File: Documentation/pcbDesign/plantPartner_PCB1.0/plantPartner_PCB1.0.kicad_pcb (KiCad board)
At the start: 2 copper layers, 148.3 x 66.8 mm, 78 parts, among them IC1 MPM3610, J1 Conn_01x04, J10 Screw_Terminal_01x03, J11 Conn_01x02, J12 Conn_01x03, J13 Conn_01x03, J14 Conn_01x03, J15 Conn_01x03, J16 Conn_01x04, J17 Conn_01x03, J18 Screw_Terminal_01x02, J19 Barrel_Jack, J2 Conn_01x04, J20 Conn_02x04_Top_Bottom, J21 Conn_01x04, J22 Conn_01x04, J23 Conn_01x01, J24 Conn_01x03, J25 Conn_01x03, J26 Conn_01x01, J27 Conn_01x01, J28 Conn_01x01, J29 Conn_01x02, J3 Conn_01x04, J4 Screw_Terminal, J5 Conn_01x02, J6 Screw_Terminal_01x03, J7 Conn_01x03, J8 Conn_02x04_Top_Bottom, J9 Conn_01x03, K1 SRD-05VDC-SL-C, K2 SRD-05VDC-SL-C, Q1 PNP, Q2 PNP, U1 EL357N-G, U2 MAX485, U3 ESP32-DEVKIT-V1, U4 EL357N-G

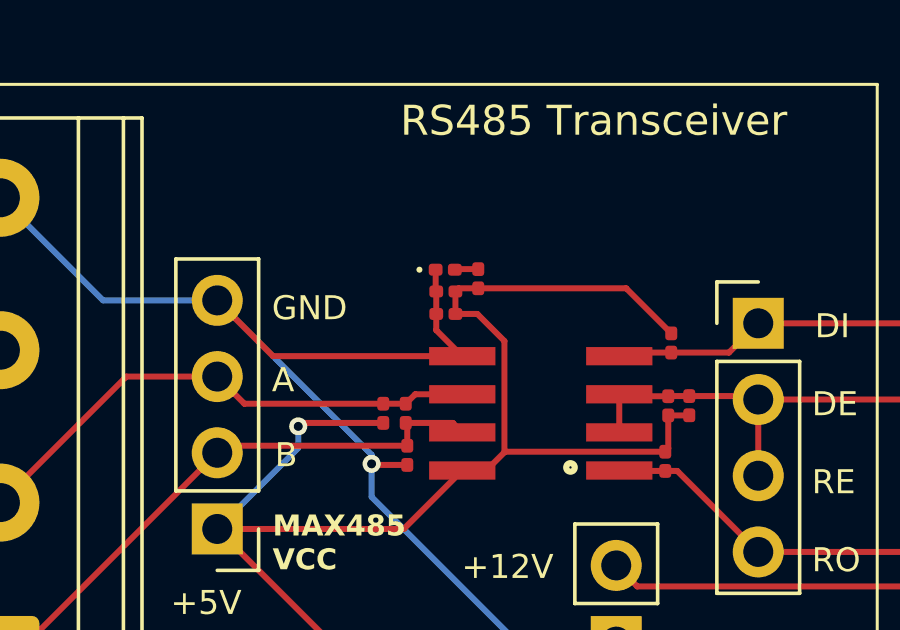
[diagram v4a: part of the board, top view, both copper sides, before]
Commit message: Meeting with Tyler. I tried to implement Lamp Circuit with MOSFET but having trouble simulating it in LTspice
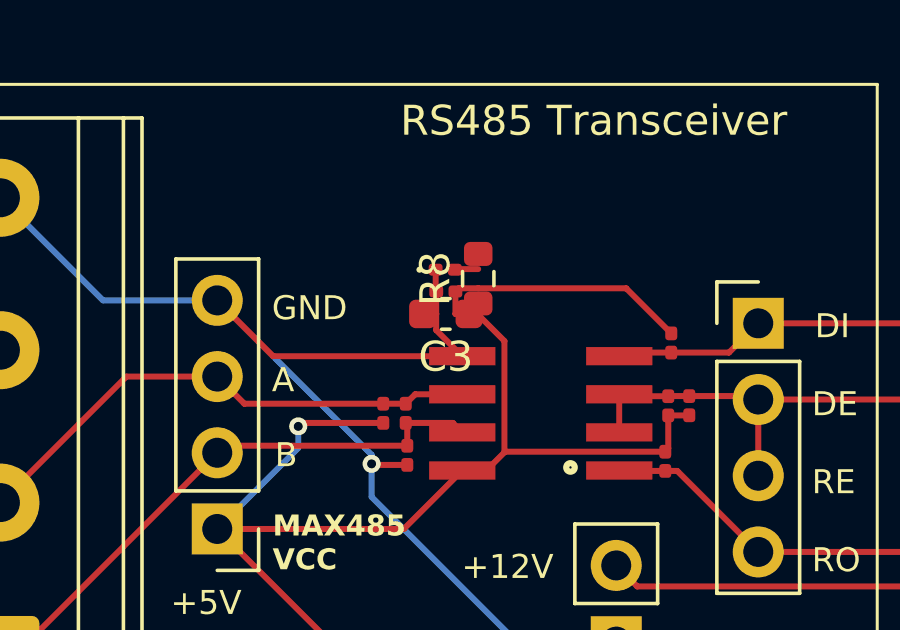
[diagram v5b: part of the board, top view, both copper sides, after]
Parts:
- C3: footprint Capacitor_SMD:C_0201_0603Metric -> Capacitor_SMD:C_0603_1608Metric
- R8: footprint Resistor_SMD:R_0201_0603Metric -> Resistor_SMD:R_0603_1608Metric
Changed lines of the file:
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@@
 		)
 	)
-	(footprint "Resistor_SMD:R_0201_0603Metric"
+	(footprint "Resistor_SMD:R_0603_1608Metric"
 		(layer "F.Cu")
 		(at 90.055 68.6275 90)
-		(descr "Resistor SMD 0201 (0603 Metric), square (rectangular) end terminal, IPC-7351 nominal, (Body size source: https://www.vishay.com/docs/20052/crcw0201e3.pdf), generated with kicad-footprint-generator")
+		(descr "Resistor SMD 0603 (1608 Metric), square (rectangular) end terminal, IPC-7351 nominal, (Body size source: IPC-SM-782 page 72, https://www.pcb-3d.com/wordpress/wp-content/uploads/ipc-sm-782a_amendment_1_and_2.pdf), generated with kicad-footprint-generator")
 		(tags "resistor")
 		(property "Reference" "R8"
-			(at 0 -1.05 90)
-			(layer "F.SilkS")
-			(hide yes)
+			(at 0 -1.43 90)
+			(layer "F.SilkS")
 			(effects
 				(font
@@
 		)
 		(property "Value" "1k"
-			(at 0 1.05 90)
+			(at 0 1.43 90)
 			(layer "F.Fab")
 			(effects
@@
 		(sheetfile "plantPartner_PCB1.0.kicad_sch")
 		(attr smd)
-		(fp_rect
-			(start -0.7 -0.35)
-			(end 0.7 0.35)
+		(fp_line
+			(start -0.237258 -0.5225)
+			(end 0.237258 -0.5225)
+			(stroke
+				(width 0.12)
+				(type solid)
+			)
+			(layer "F.SilkS")
+		)
+		(fp_line
+			(start -0.237258 0.5225)
+			(end 0.237258 0.5225)
+			(stroke
+				(width 0.12)
+				(type solid)
+			)
+			(layer "F.SilkS")
+		)
+		(fp_rect
+			(start -1.48 -0.73)
+			(end 1.48 0.73)
 			(stroke
 				(width 0.05)
@@
 		)
 		(fp_rect
-			(start -0.3 -0.15)
-			(end 0.3 0.15)
+			(start -0.8 -0.4125)
+			(end 0.8 0.4125)
 			(stroke
 				(width 0.1)
@@
 		)
 		(fp_text user "${REFERENCE}"
-			(at 0 -0.68 90)
-			(layer "F.Fab")
-			(effects
-				(font
-					(size 0.25 0.25)
-					(thickness 0.04)
-				)
-			)
-		)
-		(pad "" smd roundrect
-			(at -0.345 0 90)
-			(size 0.318 0.36)
-			(layers "F.Paste")
-			(roundrect_rratio 0.25)
-		)
-		(pad "" smd roundrect
-			(at 0.345 0 90)
-			(size 0.318 0.36)
-			(layers "F.Paste")
-			(roundrect_rratio 0.25)
+			(at 0 0 90)
+			(layer "F.Fab")
+			(effects
+				(font
+					(size 0.4 0.4)
+					(thickness 0.06)
+				)
+			)
 		)
 		(pad "1" smd roundrect
-			(at -0.32 0 90)
-			(size 0.46 0.4)
-			(layers "F.Cu" "F.Mask")
+			(at -0.825 0 90)
+			(size 0.8 0.95)
+			(layers "F.Cu" "F.Mask" "F.Paste")
 			(roundrect_rratio 0.25)
 			(net 52 "+5V")
@@
 		)
 		(pad "2" smd roundrect
-			(at 0.32 0 90)
-			(size 0.46 0.4)
-			(layers "F.Cu" "F.Mask")
+			(at 0.825 0 90)
+			(size 0.8 0.95)
+			(layers "F.Cu" "F.Mask" "F.Paste")
 			(roundrect_rratio 0.25)
 			(net 2 "Net-(D1-A)")
@@
 		)
 		(embedded_fonts no)
-		(model "${KICAD9_3DMODEL_DIR}/Resistor_SMD.3dshapes/R_0201_0603Metric.step"
+		(model "${KICAD9_3DMODEL_DIR}/Resistor_SMD.3dshapes/R_0603_1608Metric.step"
 			(offset
 				(xyz 0 0 0)
@@
 		)
 	)
-	(footprint "Capacitor_SMD:C_0201_0603Metric"
+	(footprint "Capacitor_SMD:C_0603_1608Metric"
 		(layer "F.Cu")
 		(at 88.975 69.8025 180)
-		(descr "Capacitor SMD 0201 (0603 Metric), square (rectangular) end terminal, IPC-7351 nominal, (Body size source: https://www.vishay.com/docs/20052/crcw0201e3.pdf), generated with kicad-footprint-generator")
+		(descr "Capacitor SMD 0603 (1608 Metric), square (rectangular) end terminal, IPC-7351 nominal, (Body size source: IPC-SM-782 page 76, https://www.pcb-3d.com/wordpress/wp-content/uploads/ipc-sm-782a_amendment_1_and_2.pdf), generated with kicad-footprint-generator")
 		(tags "capacitor")
 		(property "Reference" "C3"
-			(at 0 -1.05 0)
-			(layer "F.SilkS")
-			(hide yes)
+			(at 0 -1.43 180)
+			(layer "F.SilkS")
 			(effects
 				(font
@@
 		)
 		(property "Value" "10uF"
-			(at 0.285 1.05 0)
+			(at 0 1.43 180)
 			(layer "F.Fab")
 			(effects
@@
 		)
 		(property "Datasheet" "~"
-			(at 0 0 0)
+			(at 0 0 180)
 			(layer "F.Fab")
 			(hide yes)
@@
 		)
 		(property "Description" "Unpolarized capacitor"
-			(at 0 0 0)
+			(at 0 0 180)
 			(layer "F.Fab")
 			(hide yes)
@@
 		(sheetfile "plantPartner_PCB1.0.kicad_sch")
 		(attr smd)
-		(fp_rect
-			(start -0.7 -0.35)
-			(end 0.7 0.35)
+		(fp_line
+			(start -0.14058 0.51)
+			(end 0.14058 0.51)
+			(stroke
+				(width 0.12)
+				(type solid)
+			)
+			(layer "F.SilkS")
+		)
+		(fp_line
+			(start -0.14058 -0.51)
+			(end 0.14058 -0.51)
+			(stroke
+				(width 0.12)
+				(type solid)
+			)
+			(layer "F.SilkS")
+		)
+		(fp_rect
+			(start -1.48 -0.73)
+			(end 1.48 0.73)
 			(stroke
 				(width 0.05)
@@
 		)
 		(fp_rect
-			(start -0.3 -0.15)
-			(end 0.3 0.15)
+			(start -0.8 -0.4)
+			(end 0.8 0.4)
 			(stroke
 				(width 0.1)
@@
 		)
 		(fp_text user "${REFERENCE}"
-			(at 0 -0.68 0)
-			(layer "F.Fab")
-			(effects
-				(font
-					(size 0.25 0.25)
-					(thickness 0.04)
-				)
-			)
-		)
-		(pad "" smd roundrect
-			(at -0.345 0 180)
-			(size 0.318 0.36)
-			(layers "F.Paste")
-			(roundrect_rratio 0.25)
-		)
-		(pad "" smd roundrect
-			(at 0.345 0 180)
-			(size 0.318 0.36)
-			(layers "F.Paste")
-			(roundrect_rratio 0.25)
+			(at 0 0 180)
+			(layer "F.Fab")
+			(effects
+				(font
+					(size 0.4 0.4)
+					(thickness 0.06)
+				)
+			)
 		)
 		(pad "1" smd roundrect
-			(at -0.32 0 180)
-			(size 0.46 0.4)
-			(layers "F.Cu" "F.Mask")
+			(at -0.775 0 180)
+			(size 0.9 0.95)
+			(layers "F.Cu" "F.Mask" "F.Paste")
 			(roundrect_rratio 0.25)
 			(net 52 "+5V")
@@
 		)
 		(pad "2" smd roundrect
-			(at 0.32 0 180)
-			(size 0.46 0.4)
-			(layers "F.Cu" "F.Mask")
+			(at 0.775 0 180)
+			(size 0.9 0.95)
+			(layers "F.Cu" "F.Mask" "F.Paste")
 			(roundrect_rratio 0.25)
 			(net 1 "GND")
@@
 		)
 		(embedded_fonts no)
-		(model "${KICAD9_3DMODEL_DIR}/Capacitor_SMD.3dshapes/C_0201_0603Metric.step"
+		(model "${KICAD9_3DMODEL_DIR}/Capacitor_SMD.3dshapes/C_0603_1608Metric.step"
 			(offset
 				(xyz 0 0 0)

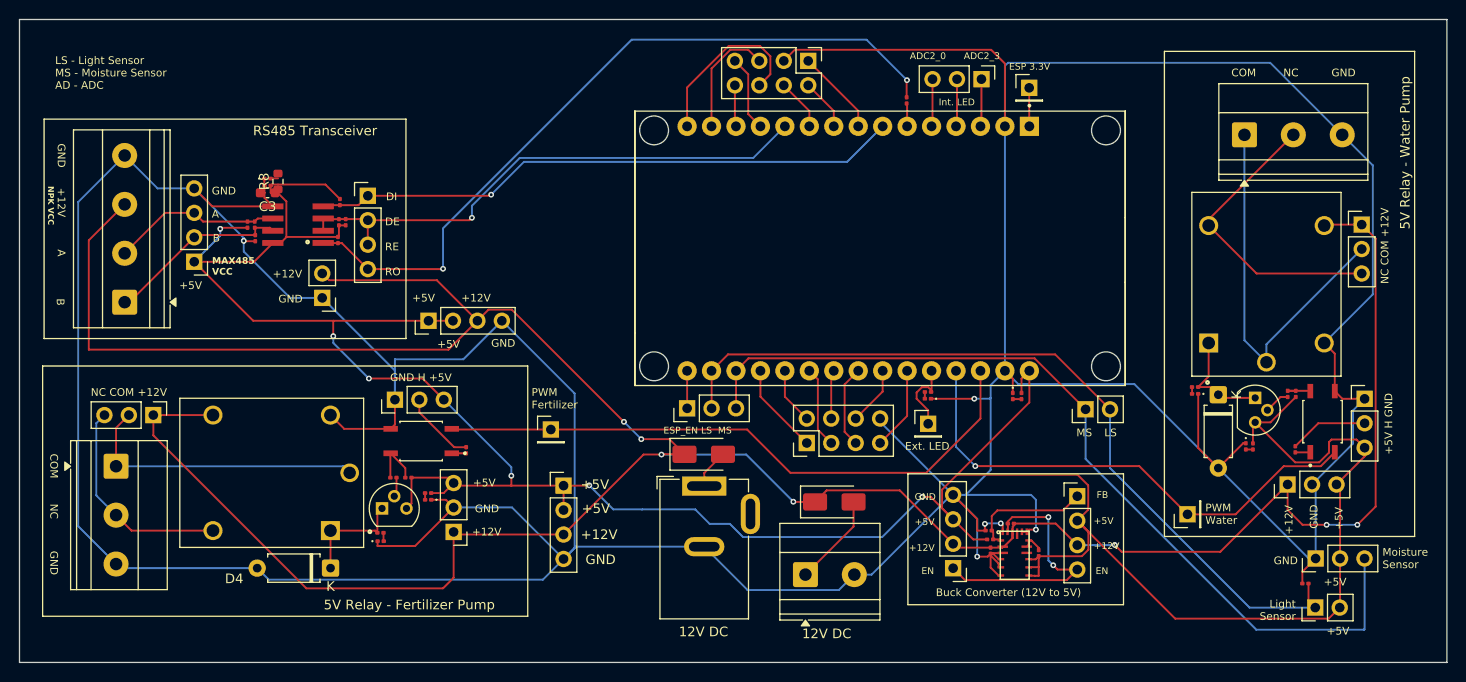
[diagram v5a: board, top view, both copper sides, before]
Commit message: Added Lamp to PCB. Added Copper Pours and Drill Holes. Now fixing rude error about cap. not getting copper pour connection properly
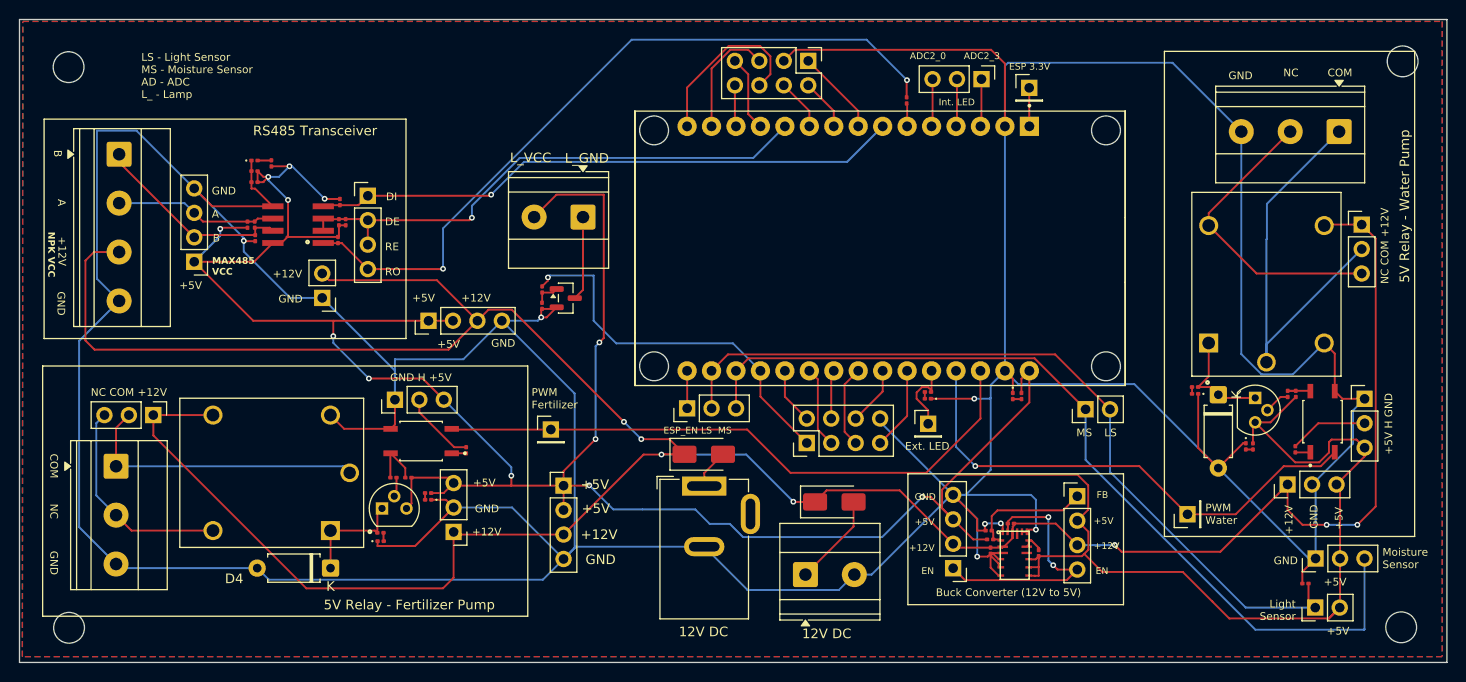
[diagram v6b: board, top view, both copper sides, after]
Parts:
- added J30: Screw_Terminal_01x02, TerminalBlock_Phoenix:TerminalBlock_Phoenix_MKDS-1,5-2-5.08_1x02_P5.08mm_Horizontal, F.Cu at (121.7, 72.3)
- added Q4: AO3400A, Package_TO_SOT_SMD:SOT-23, F.Cu at (120.0, 80.8)
- added R25: 100, Resistor_SMD:R_0201_0603Metric, F.Cu at (117.5, 79.8)
- added R27: 10k, Resistor_SMD:R_0201_0603Metric, F.Cu at (117.5, 81.5)
- added REF**: MountingHole_3.2mm_M3, MountingHole:MountingHole_3.2mm_M3, F.Cu at (68.3, 56.8)
- added REF**: MountingHole_3.2mm_M3, MountingHole:MountingHole_3.2mm_M3, F.Cu at (206.9, 56.1)
- added REF**: MountingHole_3.2mm_M3, MountingHole:MountingHole_3.2mm_M3, F.Cu at (68.3, 115.0)
- added REF**: MountingHole_3.2mm_M3, MountingHole:MountingHole_3.2mm_M3, F.Cu at (206.8, 115.0)
- C3: footprint Capacitor_SMD:C_0603_1608Metric -> Capacitor_SMD:C_0201_0603Metric
- R8: footprint Resistor_SMD:R_0603_1608Metric -> Resistor_SMD:R_0201_0603Metric
- moved J4 15.4 mm to (73.5, 65.8), turned to -90 degrees
- moved J10 9.84 mm to (200.3, 63.5), turned to 180 degrees
- moved D1 2.30 mm to (87.6, 66.5)
- moved C4 2.02 mm to (87.6, 67.5)
- moved R8 2.00 mm to (89.4, 66.8)
- moved C3 1.75 mm to (87.6, 68.7)
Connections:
- net /ADC1_6 renamed /LAMP_PIN
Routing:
- net +5V: track 298.6 -> 346.7 mm, vias 6 -> 12
- net /LAMP_PIN: track 9.49 -> 39.7 mm, vias 0 -> 1
- net GND: track 565.6 -> 583.1 mm, vias 6 -> 7
- net /Drain: track 0.00 -> 8.78 mm
- net +12V: track 307.4 -> 303.7 mm
- net /Gate: track 0.00 -> 2.73 mm
- net /COM: track 71.1 -> 73.6 mm
- net /B: track 19.2 -> 21.1 mm
- net /A: track 17.6 -> 16.9 mm
- net Net-(D1-A): track 0.79 -> 1.47 mm
- added copper zone on B.Cu, net GND
- added copper zone on F.Cu, net GND
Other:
- board text added: "AD2_7 AD2_8 AD1_4 L_PIN"
- board text added: "LS - Light Sensor MS - Moisture Sensor AD - ADC L_ - Lamp"
- board text added: "L_GND"
- board text added: "L_VCC"
- board text added: "R25"
- board text removed: "AD2_7 AD2_8 AD1_4 AD1_6"
- board text removed: "LS - Light Sensor MS - Moisture Sensor AD - ADC"

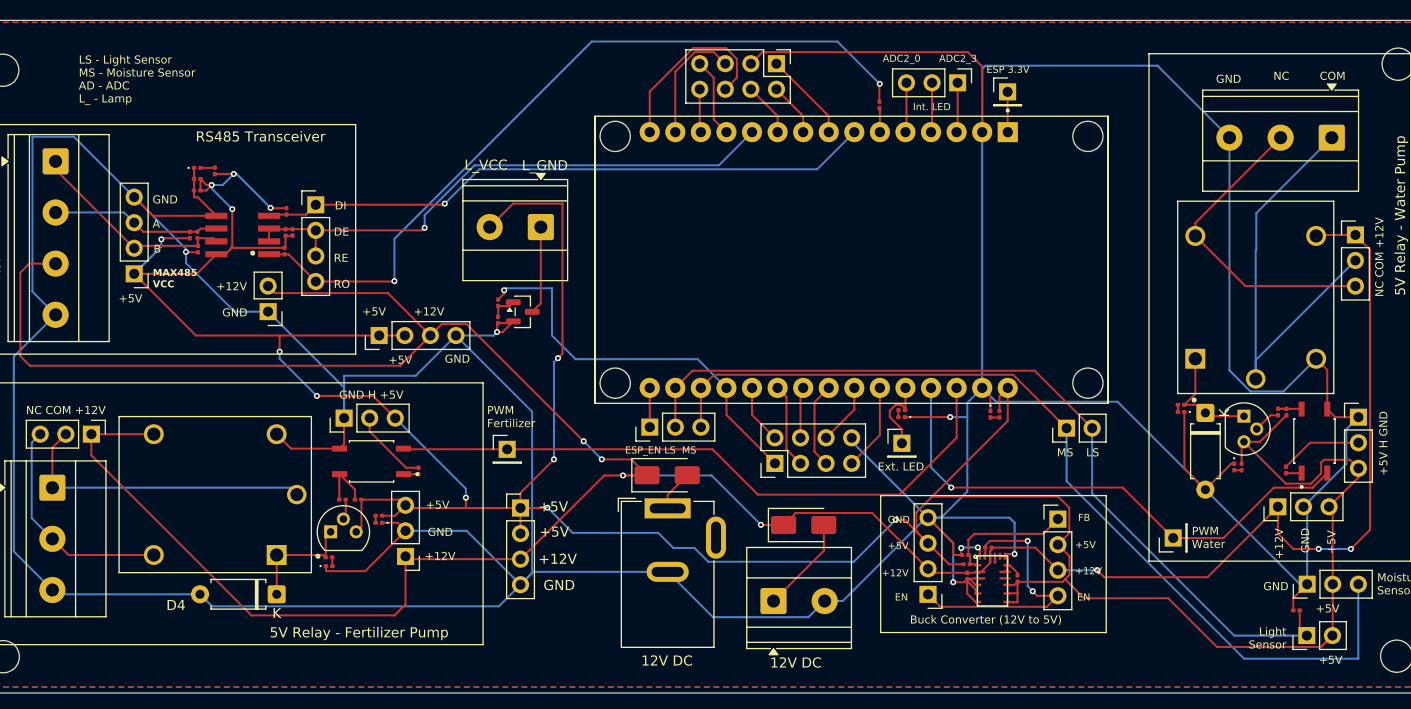
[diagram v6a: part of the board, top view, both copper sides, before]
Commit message: Gerber and Drill files have been generated. I will order on JLCPCB tomorrow morning ASAP and then finish up cube for Beta
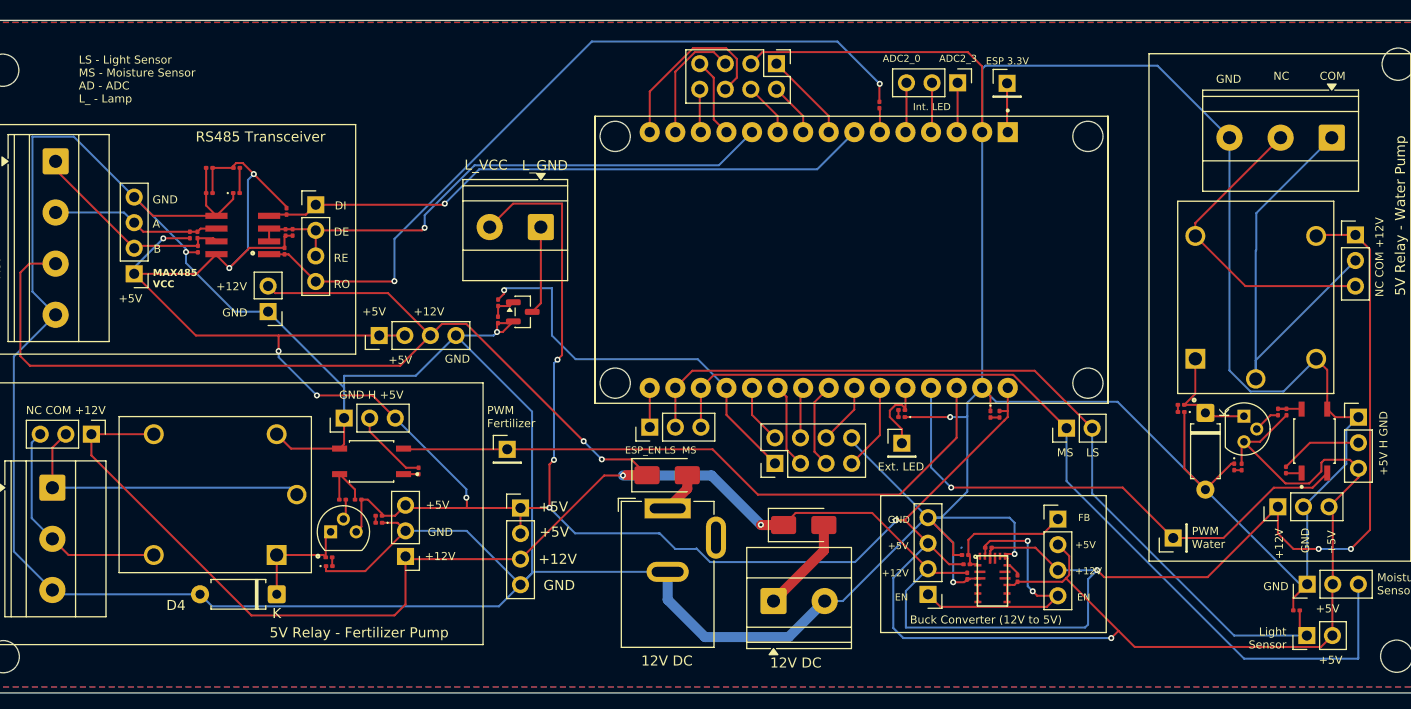
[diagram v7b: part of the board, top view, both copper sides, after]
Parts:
- moved D1 4.62 mm to (91.5, 69.0)
- moved R8 2.18 mm to (91.5, 66.5), turned to 0 degrees
- moved C4 1.63 mm to (88.8, 66.5)
- moved C3 1.23 mm to (88.8, 69.0)
- moved J28 0.85 mm to (168.1, 58.0)
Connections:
- IC1 pad 11: GND -> unconnected-(IC1-BST-Pad11)
- IC1 pad 18: GND -> unconnected-(IC1-AAM-Pad18)
- IC1 pad 2: +12V -> unconnected-(IC1-VCC-Pad2)
- IC1 pad 4: GND -> /SW
- IC1 pad 5: GND -> /SW
- IC1 pad 6: GND -> /SW
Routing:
- net +12V: track 303.7 -> 331.7 mm
- net +5V: track 346.7 -> 352.4 mm, vias 12 -> 11
- net GND: track 583.1 -> 579.2 mm, vias 7 -> 5
- net /SW: track 0.00 -> 1.70 mm
- net Net-(D1-A): track 1.47 -> 2.51 mm
- net /ESP_3.3V: track 4.01 -> 4.90 mm
